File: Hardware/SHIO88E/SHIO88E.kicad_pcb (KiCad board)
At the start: 2 copper layers, 71.5 x 79.5 mm, 140 parts, among them Q1 2N3904, Q2 2N3904, Q3 2N3904, Q4 2N3904, Q5 2N3904, Q6 2N3904, Q7 2N3904, Q8 2N3904, U1 MCP23017_SS

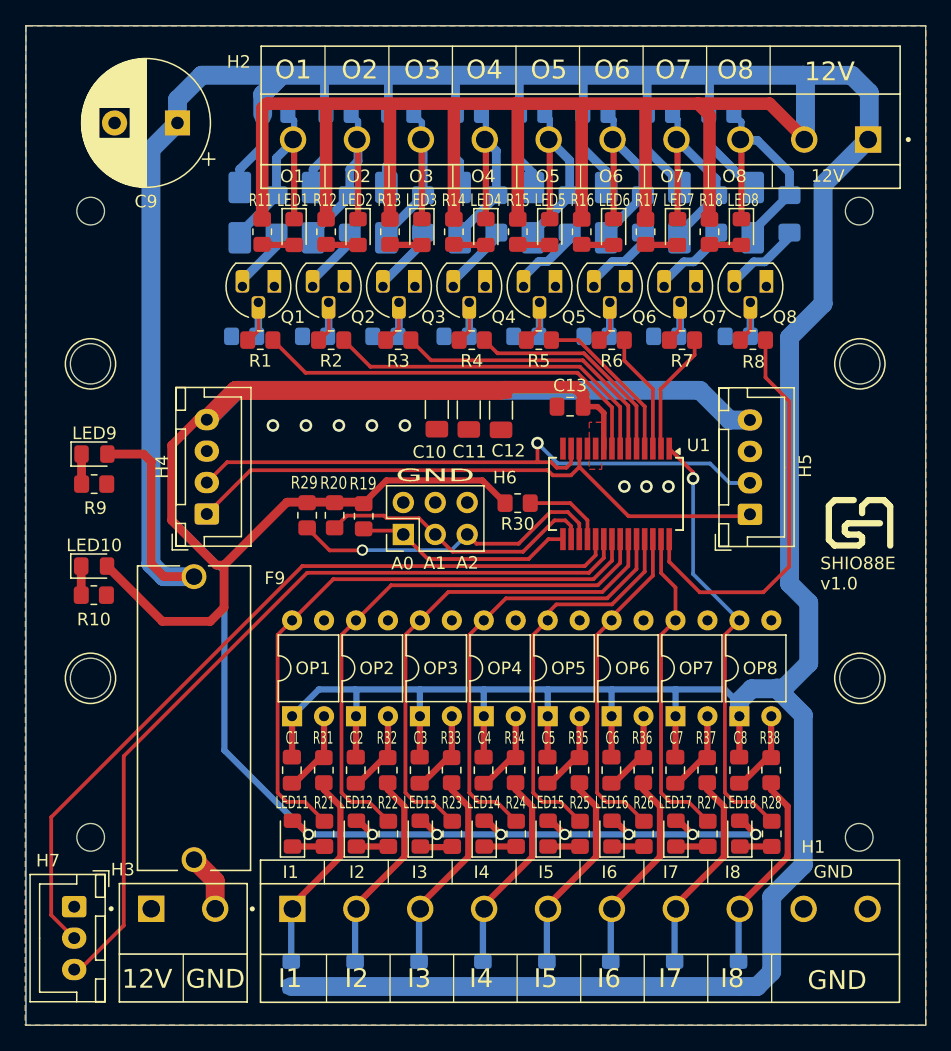
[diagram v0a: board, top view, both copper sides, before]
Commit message: GWHMI: updated symbol fields SHIO88E: fixed silkscreen texts
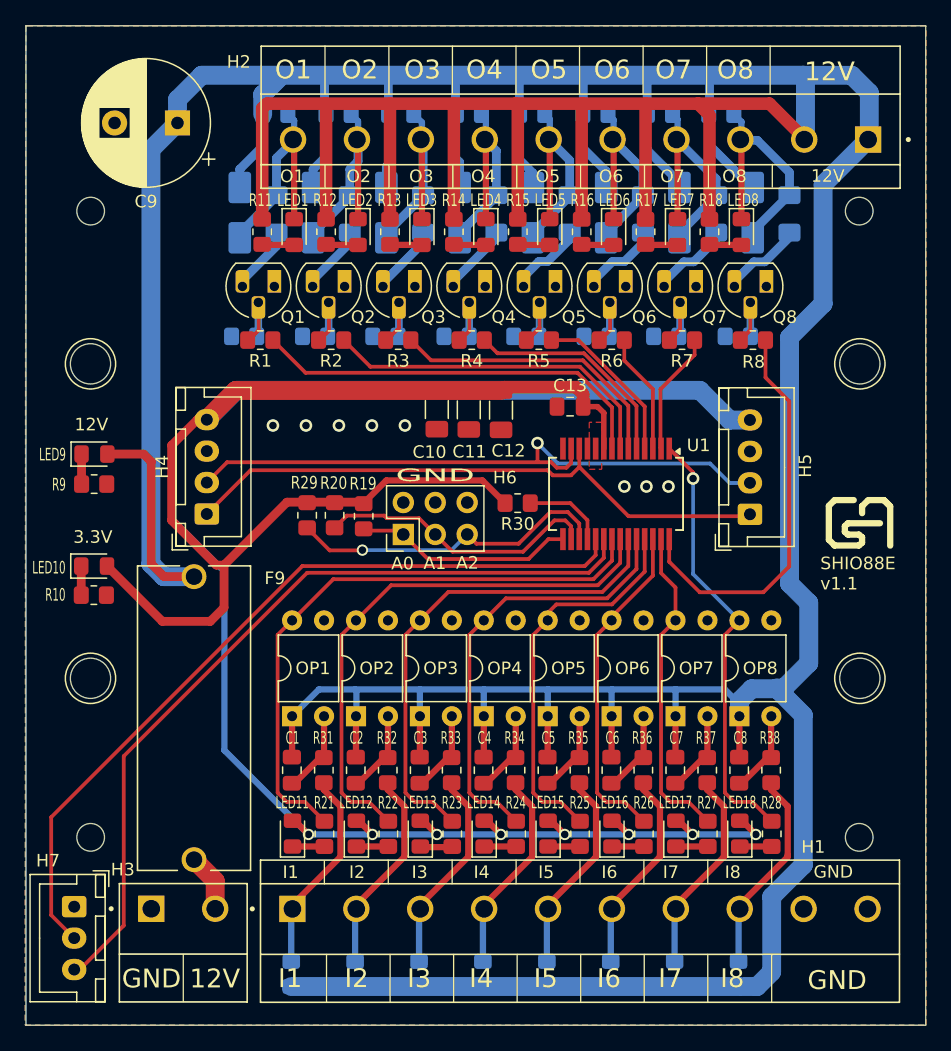
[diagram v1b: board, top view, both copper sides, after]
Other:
- board text added: "3.3V"
- board text added: "SHIO88E v1.1"
- board text removed: "SHIO88E v1.0"
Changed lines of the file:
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@@
 		(tags "LED handsolder")
 		(property "Reference" "LED10"
-			(at 0 -1.65 0)
+			(at -3.596715 0.1268 0)
 			(layer "F.SilkS")
 			(effects
 				(font
-					(size 1 1)
+					(size 1 0.6)
 					(thickness 0.15)
 				)
@@
 		(tags "resistor handsolder")
 		(property "Reference" "R10"
-			(at 0 1.9326 0)
+			(at -3.059929 -0.0256 0)
 			(layer "F.SilkS")
 			(effects
 				(font
-					(size 1 1)
+					(size 1 0.6)
 					(thickness 0.15)
 				)
@@
 		(tags "LED handsolder")
 		(property "Reference" "LED9"
-			(at 0 -1.65 0)
+			(at -3.3364 0.0408 0)
 			(layer "F.SilkS")
 			(effects
 				(font
-					(size 1 1)
+					(size 1 0.6)
 					(thickness 0.15)
 				)
@@
 		(tags "resistor handsolder")
 		(property "Reference" "R9"
-			(at 0.0958 1.9072 0)
+			(at -2.799615 0.0408 0)
 			(layer "F.SilkS")
 			(effects
 				(font
-					(size 1 1)
+					(size 1 0.6)
 					(thickness 0.15)
 				)
@@
 	)
 	(gr_text "GND"
-		(at 68.0466 116.0526 0)
+		(at 63.0174 116.0526 0)
 		(layer "B.SilkS")
 		(effects
@@
 	)
 	(gr_text "12V"
-		(at 62.9666 116.0526 0)
+		(at 68.4276 116.0526 0)
 		(layer "B.SilkS")
 		(effects
@@
 	)
 	(gr_text "GND"
-		(at 68.0974 118.3894 0)
+		(at 63.0174 118.364 0)
 		(layer "F.SilkS")
 		(effects
@@
 	)
 	(gr_text "12V"
-		(at 63.0174 118.3894 0)
+		(at 68.4022 118.364 0)
 		(layer "F.SilkS")
 		(effects
@@
 		)
 	)
+	(gr_text "3.3V"
+		(at 59.1566 82.9564 0)
+		(layer "F.SilkS")
+		(effects
+			(font
+				(size 1 1)
+				(thickness 0.15)
+			)
+			(justify left bottom)
+		)
+	)
 	(gr_text "O1"
 		(at 75.184 46.101 0)
@@
 		)
 	)
+	(gr_text "12V"
+		(at 59.2582 74.0156 0)
+		(layer "F.SilkS")
+		(effects
+			(font
+				(size 1 1)
+				(thickness 0.15)
+			)
+			(justify left bottom)
+		)
+	)
 	(gr_text "I7"
 		(at 105.664 118.3386 0)
@@
 		)
 	)
-	(gr_text "SHIO88E\nv1.0"
+	(gr_text "SHIO88E\nv1.1"
 		(at 118.5418 86.6648 0)
 		(layer "F.SilkS")
